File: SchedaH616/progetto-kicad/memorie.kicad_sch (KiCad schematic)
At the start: 54 parts, among them J401 DM3AT-SF-PEJM5, U401 K4AAG165WA-BCWE, U402 FEMDNN064G-C9A61, U403 TPD4E05U06DQA, U404 TPD4E05U06DQA

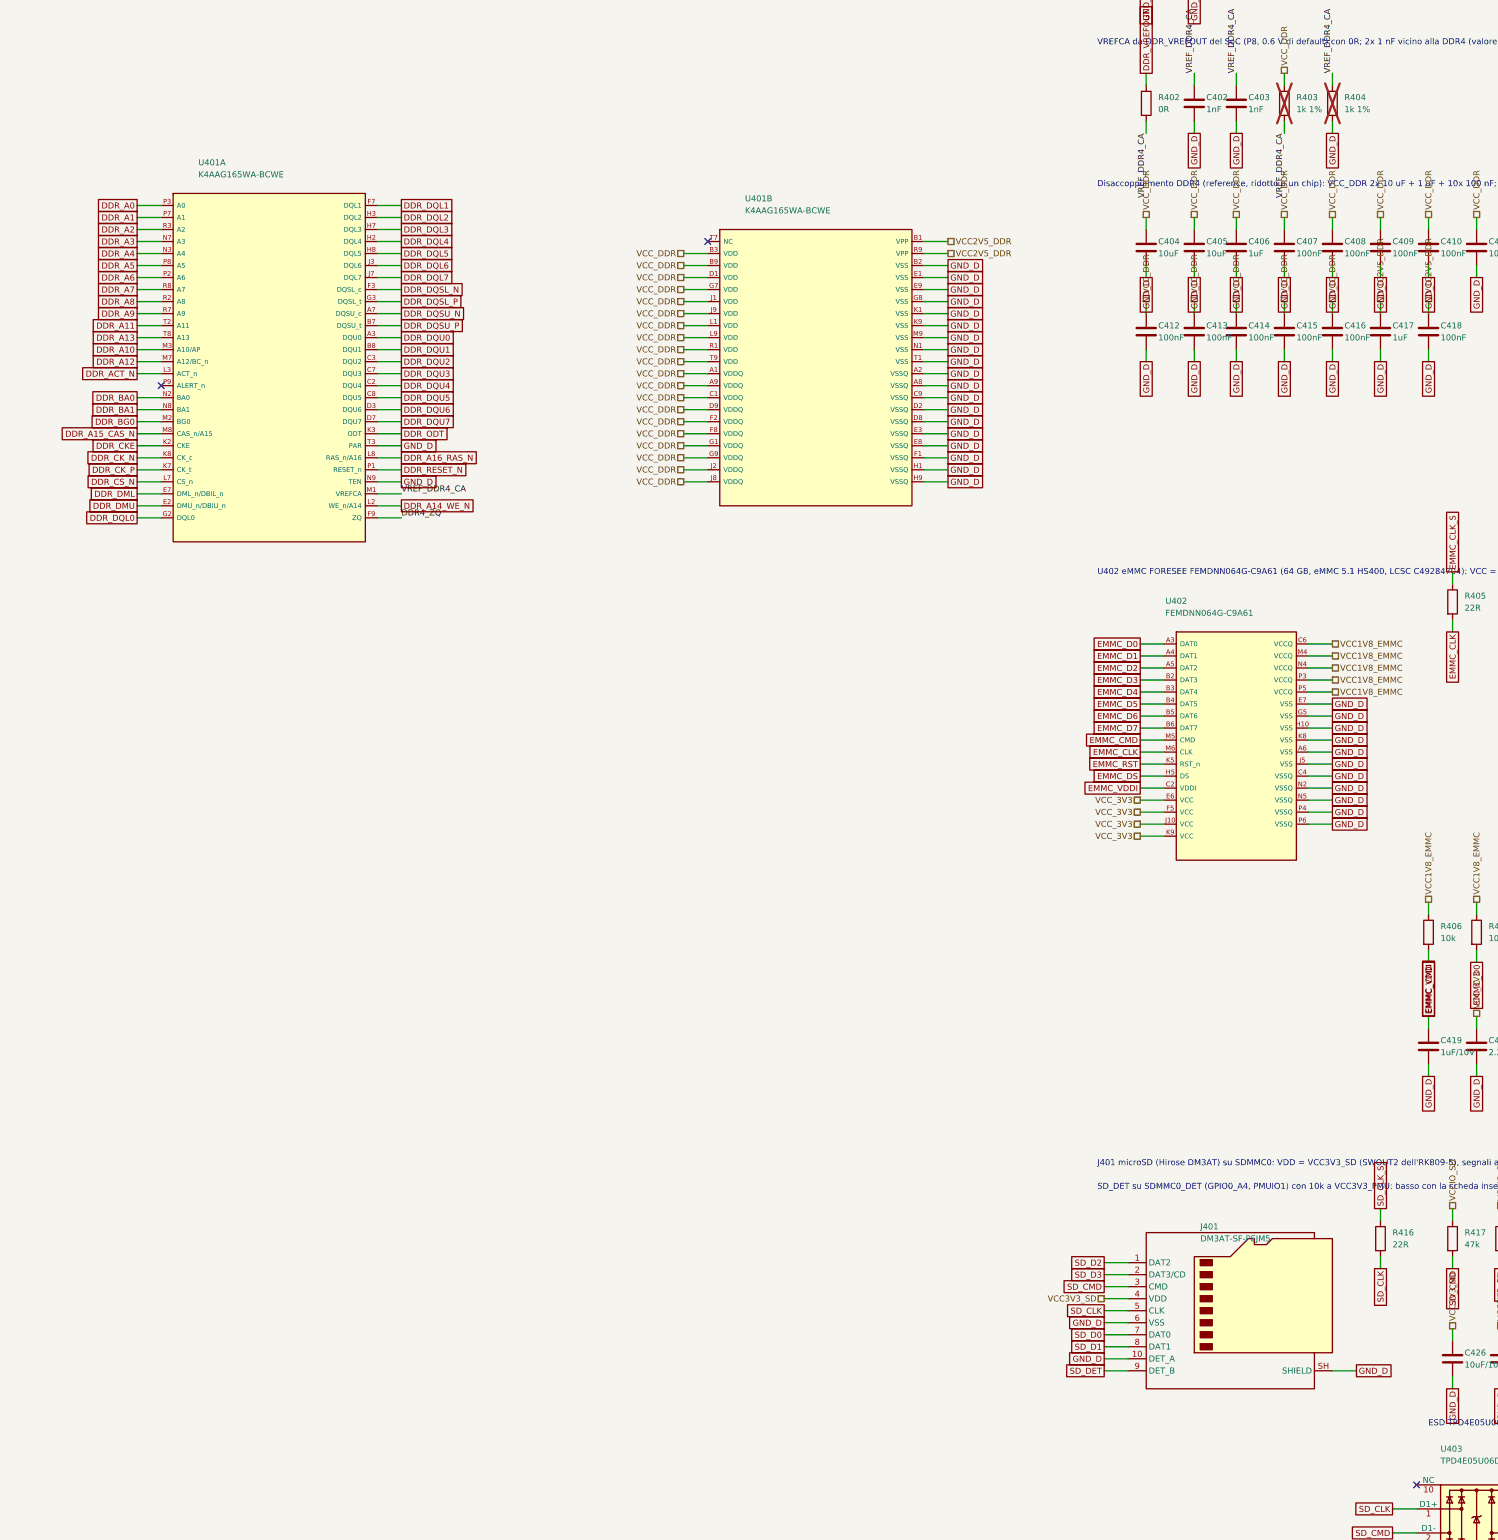
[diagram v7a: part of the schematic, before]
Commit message: SchedaH616: componenti specifici dalla libreria MIKILAB
- simbolo e footprint MIKILAB per RK809-5, TCS4525, K4AAG165WA-BCWE, FEMDNN064G-C9A61,
  AP2112K-1.8TRG1, TPS56637RPAR, TPS2121RUXR, SY6280AAC, TPS563201DDCR, TPS2553DBVR,
  TYPE-C-31-M-12, FH12-30S-0.5SH, FPC-05F-28PH20, HR911130C, 25AA02E48T-I/OT, DM3AT-SF-PEJM5;
  simbolo MIKILAB per l'AP6256
- restano nella libreria di progetto: RK3568 (pad EasyEDA da 0.35 mm, niente fanout 5/5 mil),
  simbolo RTL8211F (quello MIKILAB ha pin di alimentazione nascosti), footprint AP6256 LGA-47,
  portapila BS-12; motivazioni in docs/scelte-progetto.md
- kilib.mik() carica simboli e footprint dalla libreria (variabile MIKILAB); matrice ERC:
  pin unspecified dei simboli EasyEDA OK
- netlist identica a 4ca35fc (439 componenti, 314 net); ERC 0, parita' 0, DRC 0 (solo
  collegamenti da fare); footprint corretti nella libreria MIKILAB 8b990c4

Co-Authored-By: Claude Opus 5.5 (1M context) <noreply@anthropic.com>
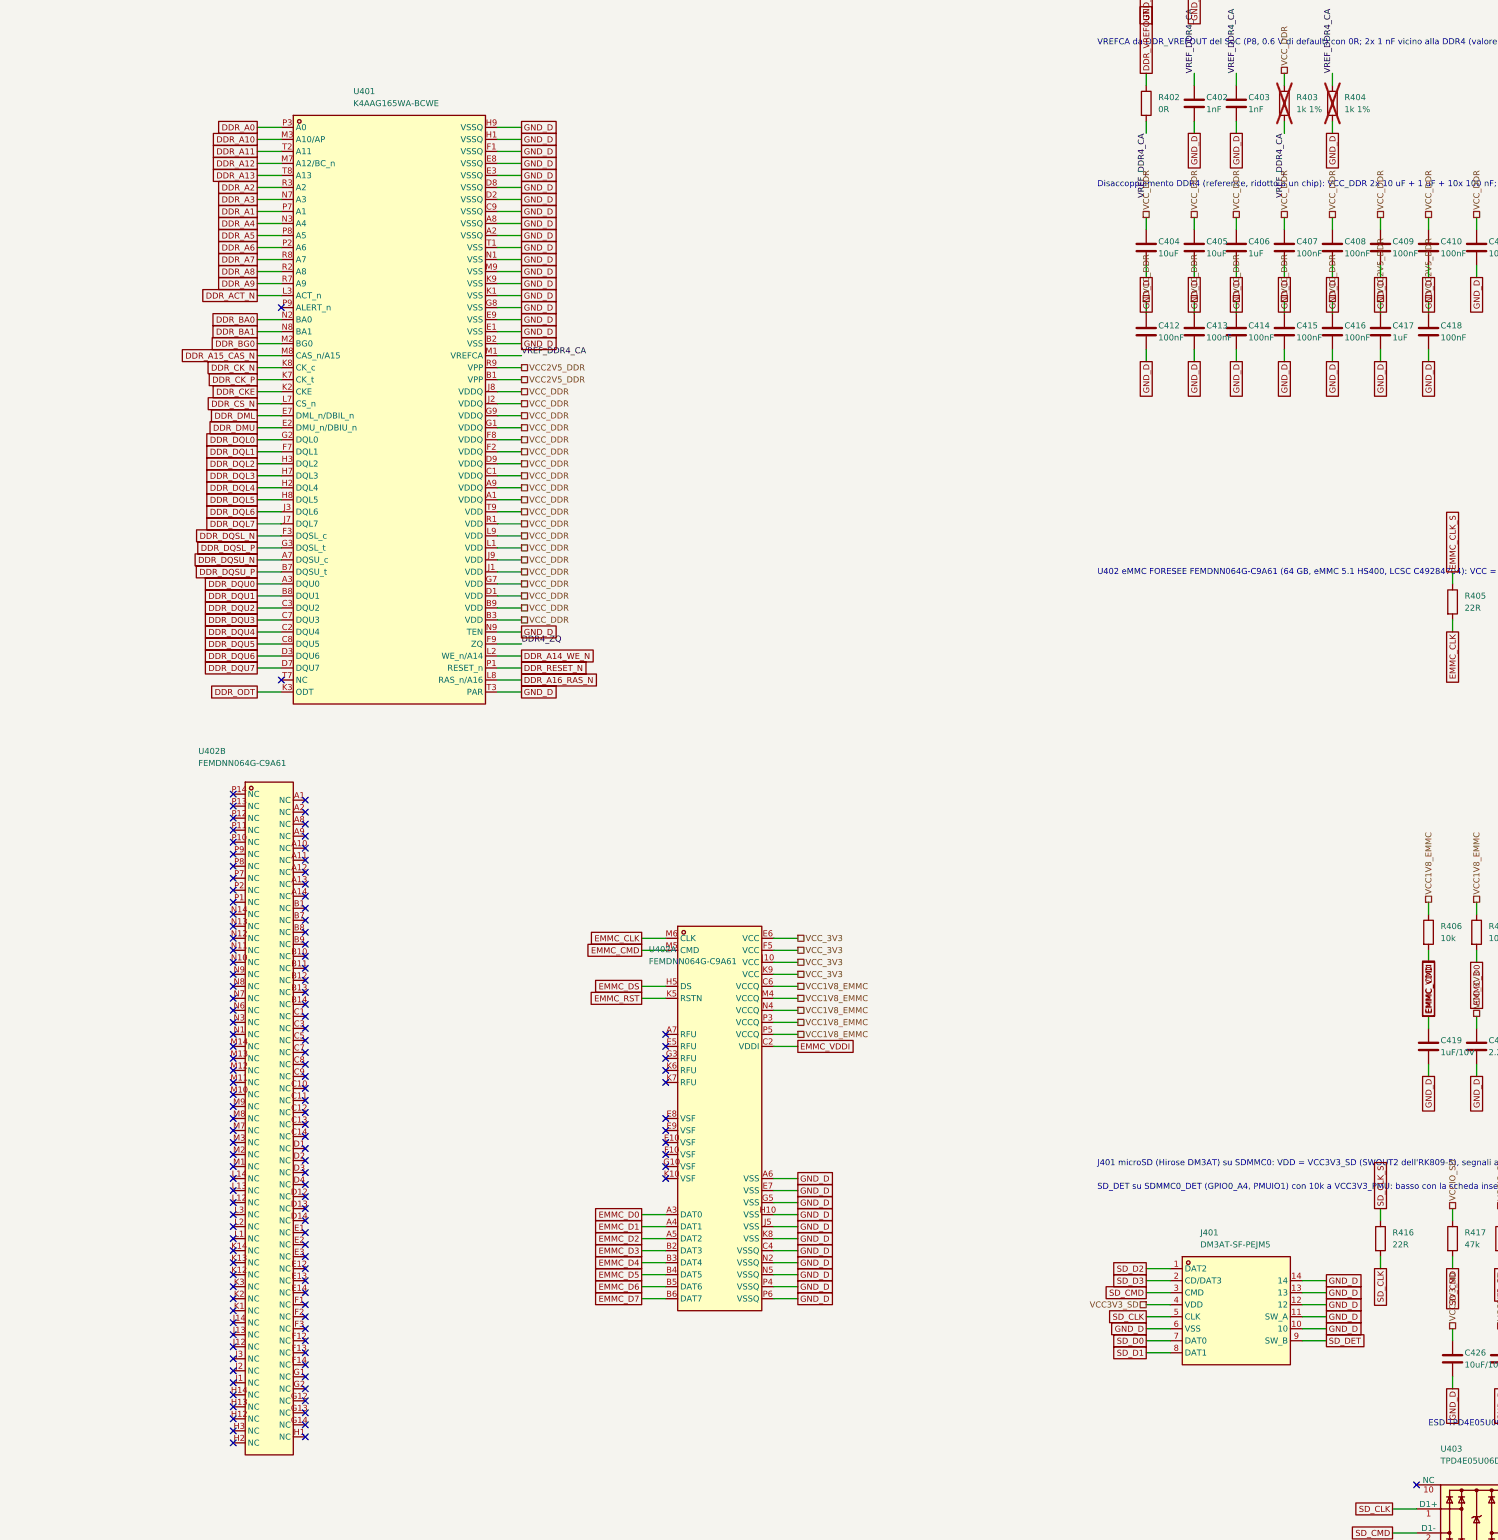
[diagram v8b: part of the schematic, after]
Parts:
- removed J401: DM3AT-SF-PEJM5, Connector_Card:microSD_HC_Hirose_DM3AT-SF-PEJM5, symbol Connector:Micro_SD_Card_Det_Hirose_DM3AT
- removed U401: K4AAG165WA-BCWE, Package_BGA:BGA-96_9.0x13.0mm_Layout2x3x16_P0.8mm, symbol Scheda:DDR4_x16_FBGA96
- removed U402: FEMDNN064G-C9A61, Package_BGA:LFBGA-153_11.5x13mm_Layout14x14_P0.5mm, symbol Scheda:eMMC_FBGA153
- added J401: DM3AT-SF-PEJM5, MIKILAB_DM3AT_SF_PEJM5:SD-SMD_DM3AT-SF-PEJM5, symbol MIKILAB_DM3AT_SF_PEJM5:DM3AT-SF-PEJM5
- added U401: K4AAG165WA-BCWE, MIKILAB_K4AAG165WA_BCWE:BGA-96_L13.3-W10.3-P0.80_K4AAG165WA-BCWE, symbol MIKILAB_K4AAG165WA_BCWE:K4AAG165WA-BCWE
- added U402: FEMDNN064G-C9A61, MIKILAB_FEMDNN064G_C9A61:BGA-153_L13.0-W11.5-P0.50-TL_FORESEE_FEMDME, symbol MIKILAB_FEMDNN064G_C9A61:FEMDNN064G-C9A61
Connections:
- net DDR4_ZQ: now also U401.F9 (ZQ)
- net DDR_A0: now also U401.P3 (A0)
- net DDR_A1: now also U401.P7 (A1)
- net DDR_A10: now also U401.M3 (A10/AP)
- net DDR_A11: now also U401.T2 (A11)
- net DDR_A12: now also U401.M7 (A12/BC_n)
- net DDR_A13: now also U401.T8 (A13)
- net DDR_A14_WE_N: now also U401.L2 (WE_n/A14)
- net DDR_A15_CAS_N: now also U401.M8 (CAS_n/A15)
- net DDR_A16_RAS_N: now also U401.L8 (RAS_n/A16)
- net DDR_A2: now also U401.R3 (A2)
- net DDR_A3: now also U401.N7 (A3)
- net DDR_A4: now also U401.N3 (A4)
- net DDR_A5: now also U401.P8 (A5)
- net DDR_A6: now also U401.P2 (A6)
- net DDR_A7: now also U401.R8 (A7)
- net DDR_A8: now also U401.R2 (A8)
- net DDR_A9: now also U401.R7 (A9)
- net DDR_ACT_N: now also U401.L3 (ACT_n)
- net DDR_BA0: now also U401.N2 (BA0)
- net DDR_BA1: now also U401.N8 (BA1)
- net DDR_BG0: now also U401.M2 (BG0)
- net DDR_CKE: now also U401.K2 (CKE)
- net DDR_CK_N: now also U401.K8 (CK_c)
- net DDR_CK_P: now also U401.K7 (CK_t)
- net DDR_CS_N: now also U401.L7 (CS_n)
- net DDR_DML: now also U401.E7 (DML_n/DBIL_n)
- net DDR_DMU: now also U401.E2 (DMU_n/DBIU_n)
- net DDR_DQL0: now also U401.G2 (DQL0)
- net DDR_DQL1: now also U401.F7 (DQL1)
- net DDR_DQL2: now also U401.H3 (DQL2)
- net DDR_DQL3: now also U401.H7 (DQL3)
- net DDR_DQL4: now also U401.H2 (DQL4)
- net DDR_DQL5: now also U401.H8 (DQL5)
- net DDR_DQL6: now also U401.J3 (DQL6)
- net DDR_DQL7: now also U401.J7 (DQL7)
- net DDR_DQSL_N: now also U401.F3 (DQSL_c)
- net DDR_DQSL_P: now also U401.G3 (DQSL_t)
- net DDR_DQSU_N: now also U401.A7 (DQSU_c)
- net DDR_DQSU_P: now also U401.B7 (DQSU_t)
- net DDR_DQU0: now also U401.A3 (DQU0)
- net DDR_DQU1: now also U401.B8 (DQU1)
- net DDR_DQU2: now also U401.C3 (DQU2)
- net DDR_DQU3: now also U401.C7 (DQU3)
- net DDR_DQU4: now also U401.C2 (DQU4)
- net DDR_DQU5: now also U401.C8 (DQU5)
- net DDR_DQU6: now also U401.D3 (DQU6)
- net DDR_DQU7: now also U401.D7 (DQU7)
- net DDR_ODT: now also U401.K3 (ODT)
- net DDR_RESET_N: now also U401.P1 (RESET_n)
- net EMMC_CLK: now also U402.M6 (CLK)
- net EMMC_CMD: now also U402.M5 (CMD)
- net EMMC_D0: now also U402.A3 (DAT0)
- net EMMC_D1: now also U402.A4 (DAT1)
- net EMMC_D2: now also U402.A5 (DAT2)
- net EMMC_D3: now also U402.B2 (DAT3)
- net EMMC_D4: now also U402.B3 (DAT4)
- net EMMC_D5: now also U402.B4 (DAT5)
- net EMMC_D6: now also U402.B5 (DAT6)
- net EMMC_D7: now also U402.B6 (DAT7)
- net EMMC_DS: now also U402.H5 (DS)
- net EMMC_RST: now also U402.K5 (RSTN)
- net EMMC_VDDI: now also U402.C2 (VDDI)
- net GND_D: now also J401.10, J401.11 (SW_A), J401.12, J401.13, J401.14, J401.6 (VSS), U401.A2 (VSSQ), U401.A8 (VSSQ), U401.B2 (VSS), U401.C9 (VSSQ), U401.D2 (VSSQ), U401.D8 (VSSQ), U401.E1 (VSS), U401.E3 (VSSQ), U401.E8 (VSSQ), U401.E9 (VSS), U401.F1 (VSSQ), U401.G8 (VSS), U401.H1 (VSSQ), U401.H9 (VSSQ), U401.K1 (VSS), U401.K9 (VSS), U401.M9 (VSS), U401.N1 (VSS), U401.N9 (TEN), U401.T1 (VSS), U401.T3 (PAR), U402.A6 (VSS), U402.C4 (VSSQ), U402.E7 (VSS), U402.G5 (VSS), U402.H10 (VSS), U402.J5 (VSS), U402.K8 (VSS), U402.N2 (VSSQ), U402.N5 (VSSQ), U402.P4 (VSSQ), U402.P6 (VSSQ)
- net SD_CLK: now also J401.5 (CLK)
- net SD_CMD: now also J401.3 (CMD)
- net SD_D0: now also J401.7 (DAT0)
- net SD_D1: now also J401.8 (DAT1)
- net SD_D2: now also J401.1 (DAT2)
- net SD_D3: now also J401.2 (CD/DAT3)
- net SD_DET: now also J401.9 (SW_B)
- net VCC1V8_EMMC: now also U402.C6 (VCCQ), U402.M4 (VCCQ), U402.N4 (VCCQ), U402.P3 (VCCQ), U402.P5 (VCCQ)
- net VCC2V5_DDR: now also U401.B1 (VPP), U401.R9 (VPP)
- net VCC3V3_SD: now also J401.4 (VDD)
- net VCC_3V3: now also U402.E6 (VCC), U402.F5 (VCC), U402.J10 (VCC), U402.K9 (VCC)
- net VCC_DDR: now also U401.A1 (VDDQ), U401.A9 (VDDQ), U401.B3 (VDD), U401.B9 (VDD), U401.C1 (VDDQ), U401.D1 (VDD), U401.D9 (VDDQ), U401.F2 (VDDQ), U401.F8 (VDDQ), U401.G1 (VDDQ), U401.G7 (VDD), U401.G9 (VDDQ), U401.J1 (VDD), U401.J2 (VDDQ), U401.J8 (VDDQ), U401.J9 (VDD), U401.L1 (VDD), U401.L9 (VDD), U401.R1 (VDD), U401.T9 (VDD)
- net VREF_DDR4_CA: now also U401.M1 (VREFCA)
- no-connect marks 11 -> 131
